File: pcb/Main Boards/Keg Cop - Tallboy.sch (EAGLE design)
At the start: 14 parts, among them X1 RJ45-8X, X2 RJ45-8X

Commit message: Rename files
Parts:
- added ROOM: 3-PIN, Donnie:HDR-3
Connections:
- removed net KEG7: D32.IO22, X2.7
- removed net KEG8: D32.IO23, X2.8
- net 5V: now also ROOM.2, X2.7
- net COOL: now also RELAY.3; no longer RELAY.2
- net GND: now also ROOM.1, X2.8
- net RDAT: now also ROOM.3
- net SOL: now also RELAY.2; no longer RELAY.3
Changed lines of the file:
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@@
 <part name="X2" library="con-tycoelectronics" library_urn="urn:adsk.eagle:library:193" deviceset="RJ45" device="" package3d_urn="urn:adsk.eagle:package:10660/1" technology="-8X"/>
 <part name="X1" library="con-tycoelectronics" library_urn="urn:adsk.eagle:library:193" deviceset="RJ45" device="" package3d_urn="urn:adsk.eagle:package:10660/1" technology="-8X"/>
+<part name="ROOM" library="Donnie" deviceset="HDR-3" device="" value="3-PIN"/>
 </parts>
 <sheets>
@@
 <attribute name="NAME" x="-63.5" y="50.8" size="1.778" layer="95" rot="R180"/>
 <attribute name="VALUE" x="-63.5" y="76.708" size="1.778" layer="96" rot="R180"/>
+</instance>
+<instance part="ROOM" gate="G$1" x="-66.04" y="15.24" smashed="yes">
+<attribute name="VALUE" x="-67.31" y="10.16" size="1.778" layer="96"/>
+<attribute name="NAME" x="-67.31" y="23.622" size="1.778" layer="95"/>
 </instance>
 </instances>
@@
 <pinref part="X1" gate="G$1" pin="8"/>
 <wire x1="-48.26" y1="71.12" x2="-63.5" y2="71.12" width="0.1524" layer="91"/>
+<wire x1="15.24" y1="35.56" x2="15.24" y2="15.24" width="0.1524" layer="91"/>
+<wire x1="15.24" y1="15.24" x2="93.98" y2="15.24" width="0.1524" layer="91"/>
+<wire x1="93.98" y1="15.24" x2="93.98" y2="60.96" width="0.1524" layer="91"/>
+<pinref part="X2" gate="G$1" pin="7"/>
+<wire x1="111.76" y1="60.96" x2="93.98" y2="60.96" width="0.1524" layer="91"/>
+<label x="106.68" y="60.96" size="1.778" layer="95"/>
+<wire x1="-5.08" y1="30.48" x2="-5.08" y2="22.86" width="0.1524" layer="91"/>
+<junction x="-5.08" y="30.48"/>
+<wire x1="-5.08" y1="22.86" x2="-45.72" y2="22.86" width="0.1524" layer="91"/>
+<wire x1="-45.72" y1="22.86" x2="-45.72" y2="17.78" width="0.1524" layer="91"/>
+<pinref part="ROOM" gate="G$1" pin="2"/>
+<wire x1="-45.72" y1="17.78" x2="-58.42" y2="17.78" width="0.1524" layer="91"/>
 </segment>
 </net>
@@
 <junction x="-15.24" y="88.9"/>
 <pinref part="C4" gate="G$1" pin="2"/>
-<wire x1="-15.24" y1="17.78" x2="-15.24" y2="53.34" width="0.1524" layer="91"/>
+<wire x1="-15.24" y1="17.78" x2="-15.24" y2="20.32" width="0.1524" layer="91"/>
+<wire x1="-15.24" y1="20.32" x2="-15.24" y2="53.34" width="0.1524" layer="91"/>
 <wire x1="-15.24" y1="53.34" x2="-15.24" y2="88.9" width="0.1524" layer="91"/>
 <wire x1="15.24" y1="45.72" x2="15.24" y2="53.34" width="0.1524" layer="91"/>
@@
 <pinref part="X1" gate="G$1" pin="7"/>
 <wire x1="-53.34" y1="68.58" x2="-63.5" y2="68.58" width="0.1524" layer="91"/>
+<pinref part="X2" gate="G$1" pin="8"/>
+<wire x1="73.66" y1="71.12" x2="73.66" y2="63.5" width="0.1524" layer="91"/>
+<wire x1="73.66" y1="63.5" x2="111.76" y2="63.5" width="0.1524" layer="91"/>
+<junction x="73.66" y="71.12"/>
+<label x="106.68" y="63.5" size="1.778" layer="95"/>
+<wire x1="-15.24" y1="20.32" x2="-43.18" y2="20.32" width="0.1524" layer="91"/>
+<wire x1="-43.18" y1="20.32" x2="-43.18" y2="15.24" width="0.1524" layer="91"/>
+<junction x="-15.24" y="20.32"/>
+<pinref part="ROOM" gate="G$1" pin="1"/>
+<wire x1="-43.18" y1="15.24" x2="-58.42" y2="15.24" width="0.1524" layer="91"/>
 </segment>
 </net>
@@
 <wire x1="-48.26" y1="30.48" x2="-38.1" y2="30.48" width="0.1524" layer="91"/>
 <pinref part="X1" gate="G$1" pin="1"/>
+<pinref part="ROOM" gate="G$1" pin="3"/>
+<wire x1="-58.42" y1="20.32" x2="-48.26" y2="20.32" width="0.1524" layer="91"/>
+<wire x1="-48.26" y1="20.32" x2="-48.26" y2="30.48" width="0.1524" layer="91"/>
+<junction x="-48.26" y="30.48"/>
 </segment>
 <segment>
@@
 </segment>
 </net>
-<net name="KEG7" class="0">
-<segment>
-<pinref part="D32" gate="G$1" pin="IO22"/>
-<label x="66.04" y="66.04" size="1.778" layer="95"/>
-<wire x1="63.5" y1="66.04" x2="78.74" y2="66.04" width="0.1524" layer="91"/>
-<wire x1="78.74" y1="66.04" x2="78.74" y2="60.96" width="0.1524" layer="91"/>
-<label x="106.68" y="60.96" size="1.778" layer="95"/>
-<pinref part="X2" gate="G$1" pin="7"/>
-<wire x1="78.74" y1="60.96" x2="111.76" y2="60.96" width="0.1524" layer="91"/>
-</segment>
-</net>
-<net name="KEG8" class="0">
-<segment>
-<pinref part="D32" gate="G$1" pin="IO23"/>
-<label x="66.04" y="68.58" size="1.778" layer="95"/>
-<wire x1="63.5" y1="68.58" x2="81.28" y2="68.58" width="0.1524" layer="91"/>
-<wire x1="81.28" y1="68.58" x2="81.28" y2="63.5" width="0.1524" layer="91"/>
-<label x="106.68" y="63.5" size="1.778" layer="95"/>
-<pinref part="X2" gate="G$1" pin="8"/>
-<wire x1="81.28" y1="63.5" x2="111.76" y2="63.5" width="0.1524" layer="91"/>
-</segment>
-</net>
 <net name="KEG1" class="0">
 <segment>
-<wire x1="101.6" y1="43.18" x2="101.6" y2="45.72" width="0.1524" layer="91"/>
 <wire x1="101.6" y1="45.72" x2="111.76" y2="45.72" width="0.1524" layer="91"/>
 <label x="106.68" y="45.72" size="1.778" layer="95"/>
 <pinref part="X2" gate="G$1" pin="1"/>
+<wire x1="101.6" y1="45.72" x2="101.6" y2="40.64" width="0.1524" layer="91"/>
 <pinref part="D32" gate="G$1" pin="IO0"/>
-<wire x1="63.5" y1="40.64" x2="101.6" y2="40.64" width="0.1524" layer="91"/>
-<wire x1="101.6" y1="40.64" x2="101.6" y2="43.18" width="0.1524" layer="91"/>
+<wire x1="101.6" y1="40.64" x2="63.5" y2="40.64" width="0.1524" layer="91"/>
 <label x="66.04" y="40.64" size="1.778" layer="95"/>
 </segment>
@@
 <pinref part="X2" gate="G$1" pin="2"/>
 <wire x1="99.06" y1="48.26" x2="111.76" y2="48.26" width="0.1524" layer="91"/>
-<wire x1="99.06" y1="48.26" x2="99.06" y2="43.18" width="0.1524" layer="91"/>
 <pinref part="D32" gate="G$1" pin="IO4"/>
-<wire x1="99.06" y1="43.18" x2="63.5" y2="43.18" width="0.1524" layer="91"/>
+<wire x1="63.5" y1="43.18" x2="99.06" y2="43.18" width="0.1524" layer="91"/>
+<wire x1="99.06" y1="43.18" x2="99.06" y2="48.26" width="0.1524" layer="91"/>
 <label x="66.04" y="43.18" size="1.778" layer="95"/>
 </segment>
@@
 </segment>
 </net>
+<net name="SOL" class="0">
+<segment>
+<pinref part="RELAY" gate="1" pin="2"/>
+<wire x1="-17.78" y1="12.7" x2="-17.78" y2="25.4" width="0.1524" layer="91"/>
+<wire x1="-17.78" y1="25.4" x2="91.44" y2="25.4" width="0.1524" layer="91"/>
+<wire x1="91.44" y1="25.4" x2="91.44" y2="45.72" width="0.1524" layer="91"/>
+<pinref part="D32" gate="G$1" pin="IO16"/>
+<wire x1="91.44" y1="45.72" x2="63.5" y2="45.72" width="0.1524" layer="91"/>
+<label x="-17.78" y="12.7" size="1.778" layer="95" rot="R90"/>
+<label x="66.04" y="45.72" size="1.778" layer="95"/>
+</segment>
+</net>
 <net name="COOL" class="0">
 <segment>
+<pinref part="RELAY" gate="1" pin="3"/>
+<wire x1="-20.32" y1="12.7" x2="-20.32" y2="27.94" width="0.1524" layer="91"/>
+<wire x1="-20.32" y1="27.94" x2="22.86" y2="27.94" width="0.1524" layer="91"/>
+<wire x1="22.86" y1="27.94" x2="22.86" y2="43.18" width="0.1524" layer="91"/>
+<wire x1="22.86" y1="43.18" x2="17.78" y2="43.18" width="0.1524" layer="91"/>
+<wire x1="17.78" y1="43.18" x2="17.78" y2="48.26" width="0.1524" layer="91"/>
 <pinref part="D32" gate="G$1" pin="IO27"/>
-<wire x1="27.94" y1="48.26" x2="17.78" y2="48.26" width="0.1524" layer="91"/>
-<wire x1="17.78" y1="48.26" x2="17.78" y2="43.18" width="0.1524" layer="91"/>
-<wire x1="17.78" y1="43.18" x2="22.86" y2="43.18" width="0.1524" layer="91"/>
-<wire x1="22.86" y1="43.18" x2="22.86" y2="33.02" width="0.1524" layer="91"/>
-<pinref part="RELAY" gate="1" pin="2"/>
-<wire x1="-17.78" y1="12.7" x2="-17.78" y2="33.02" width="0.1524" layer="91"/>
-<wire x1="-17.78" y1="33.02" x2="22.86" y2="33.02" width="0.1524" layer="91"/>
+<wire x1="17.78" y1="48.26" x2="27.94" y2="48.26" width="0.1524" layer="91"/>
 <label x="20.32" y="48.26" size="1.778" layer="95"/>
-<label x="-17.78" y="12.7" size="1.778" layer="95" rot="R90"/>
-</segment>
-</net>
-<net name="SOL" class="0">
-<segment>
-<pinref part="D32" gate="G$1" pin="IO16"/>
-<wire x1="63.5" y1="45.72" x2="73.66" y2="45.72" width="0.1524" layer="91"/>
-<wire x1="73.66" y1="45.72" x2="73.66" y2="25.4" width="0.1524" layer="91"/>
-<pinref part="RELAY" gate="1" pin="3"/>
-<wire x1="73.66" y1="25.4" x2="-20.32" y2="25.4" width="0.1524" layer="91"/>
-<wire x1="-20.32" y1="25.4" x2="-20.32" y2="12.7" width="0.1524" layer="91"/>
-<label x="66.04" y="45.72" size="1.778" layer="95"/>
 <label x="-20.32" y="12.7" size="1.778" layer="95" rot="R90"/>
 </segment>

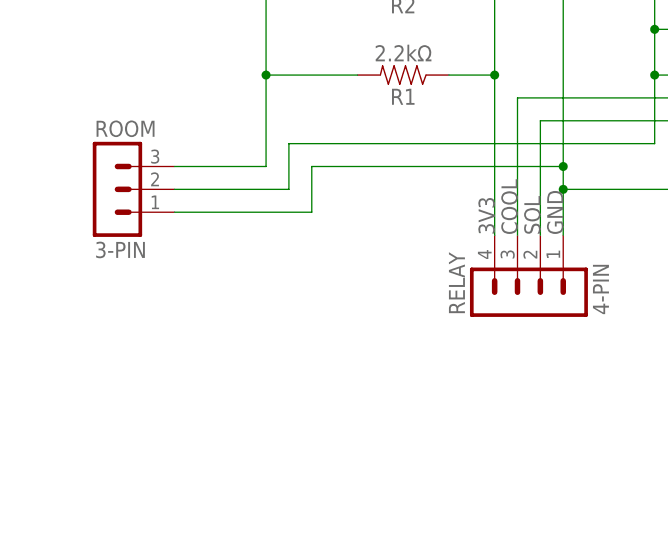
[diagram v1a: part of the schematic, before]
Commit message: Add DS18B20 sensor
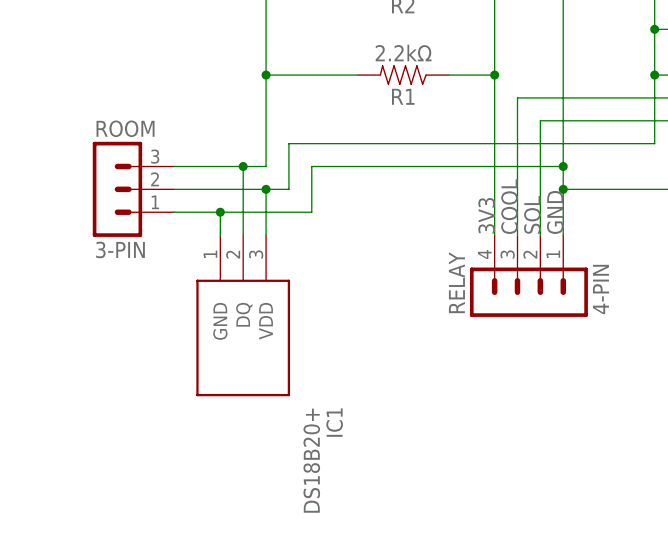
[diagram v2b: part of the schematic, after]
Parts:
- added IC1: DS18B20+, SamacSys_Parts:DS18B20+
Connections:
- net 5V: now also IC1.VDD
- net GND: now also IC1.GND
- net RDAT: now also IC1.DQ
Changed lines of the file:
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@@
 <?xml version="1.0" encoding="utf-8"?>
 <!DOCTYPE eagle SYSTEM "eagle.dtd">
-<eagle version="9.5.2">
+<eagle version="9.6.1">
 <drawing>
 <settings>
@@
 <part name="X1" library="con-tycoelectronics" library_urn="urn:adsk.eagle:library:193" deviceset="RJ45" device="" package3d_urn="urn:adsk.eagle:package:10660/1" technology="-8X"/>
 <part name="ROOM" library="Donnie" deviceset="HDR-3" device="" value="3-PIN"/>
+<part name="IC1" library="SamacSys_Parts" deviceset="DS18B20+" device=""/>
 </parts>
 <sheets>
@@
 <attribute name="VALUE" x="-67.31" y="10.16" size="1.778" layer="96"/>
 <attribute name="NAME" x="-67.31" y="23.622" size="1.778" layer="95"/>
+</instance>
+<instance part="IC1" gate="G$1" x="-48.26" y="12.7" smashed="yes" rot="R270">
+<attribute name="NAME" x="-40.64" y="-6.35" size="1.778" layer="95" rot="R270" align="center-left"/>
+<attribute name="VALUE" x="-43.18" y="-6.35" size="1.778" layer="96" rot="R270" align="center-left"/>
 </instance>
 </instances>
@@
 <wire x1="-45.72" y1="22.86" x2="-45.72" y2="17.78" width="0.1524" layer="91"/>
 <pinref part="ROOM" gate="G$1" pin="2"/>
-<wire x1="-45.72" y1="17.78" x2="-58.42" y2="17.78" width="0.1524" layer="91"/>
+<wire x1="-45.72" y1="17.78" x2="-48.26" y2="17.78" width="0.1524" layer="91"/>
+<wire x1="-48.26" y1="17.78" x2="-58.42" y2="17.78" width="0.1524" layer="91"/>
+<pinref part="IC1" gate="G$1" pin="VDD"/>
+<wire x1="-48.26" y1="12.7" x2="-48.26" y2="17.78" width="0.1524" layer="91"/>
+<junction x="-48.26" y="17.78"/>
 </segment>
 </net>
@@
 <junction x="-15.24" y="20.32"/>
 <pinref part="ROOM" gate="G$1" pin="1"/>
-<wire x1="-43.18" y1="15.24" x2="-58.42" y2="15.24" width="0.1524" layer="91"/>
+<wire x1="-43.18" y1="15.24" x2="-53.34" y2="15.24" width="0.1524" layer="91"/>
+<wire x1="-53.34" y1="15.24" x2="-58.42" y2="15.24" width="0.1524" layer="91"/>
+<pinref part="IC1" gate="G$1" pin="GND"/>
+<wire x1="-53.34" y1="12.7" x2="-53.34" y2="15.24" width="0.1524" layer="91"/>
+<junction x="-53.34" y="15.24"/>
 </segment>
 </net>
@@
 <pinref part="X1" gate="G$1" pin="1"/>
 <pinref part="ROOM" gate="G$1" pin="3"/>
-<wire x1="-58.42" y1="20.32" x2="-48.26" y2="20.32" width="0.1524" layer="91"/>
+<wire x1="-58.42" y1="20.32" x2="-50.8" y2="20.32" width="0.1524" layer="91"/>
+<wire x1="-50.8" y1="20.32" x2="-48.26" y2="20.32" width="0.1524" layer="91"/>
 <wire x1="-48.26" y1="20.32" x2="-48.26" y2="30.48" width="0.1524" layer="91"/>
 <junction x="-48.26" y="30.48"/>
+<pinref part="IC1" gate="G$1" pin="DQ"/>
+<wire x1="-50.8" y1="12.7" x2="-50.8" y2="20.32" width="0.1524" layer="91"/>
+<junction x="-50.8" y="20.32"/>
 </segment>
 <segment>
